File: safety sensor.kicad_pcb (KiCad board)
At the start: 2 copper layers, 99.1 x 45.7 mm, 29 parts, among them IC1 STM8S003F3P6, J1 Conn_01x02, J2 Conn_01x01, J3 Conn_01x01, J4 Conn_01x01, J5 Conn_01x02, J6 Conn_01x01, U1 LD1117V33, U2 VCNL3020-GS08

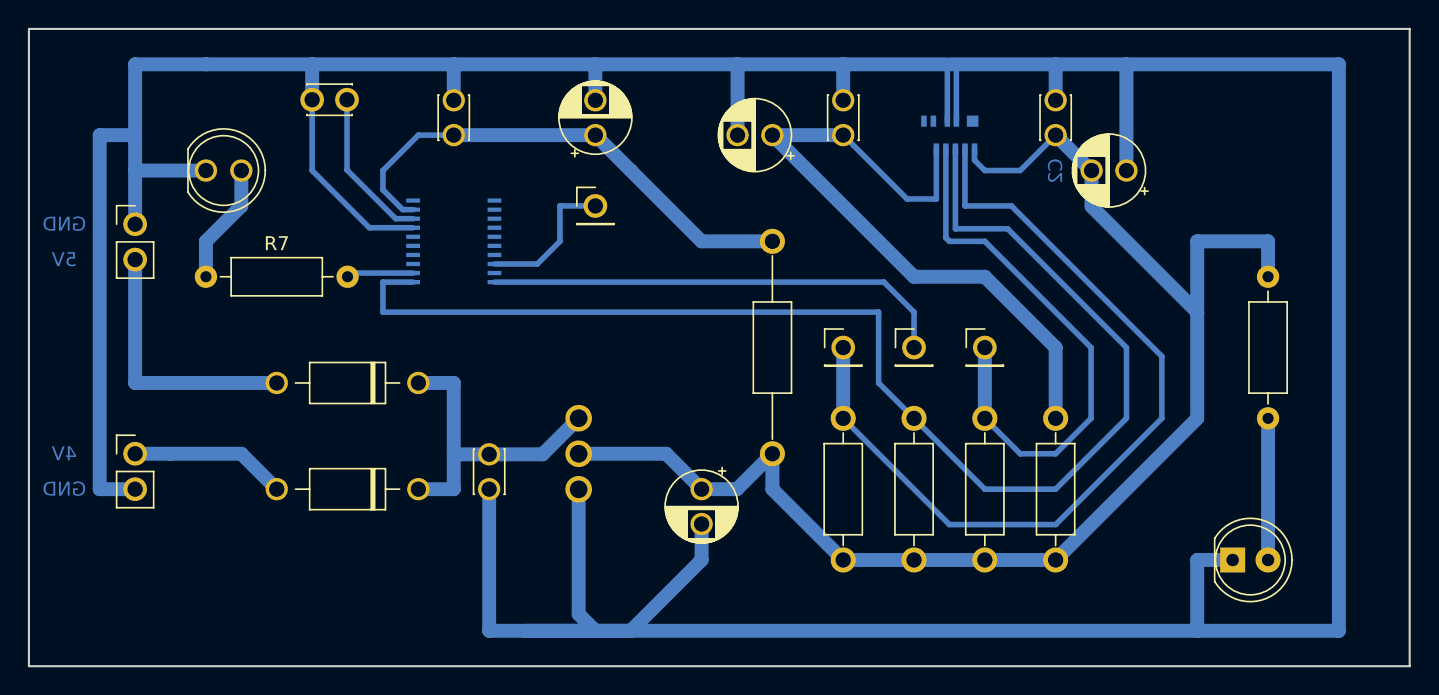
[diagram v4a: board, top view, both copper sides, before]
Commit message: fix c1 polarity, fix the hole sizes
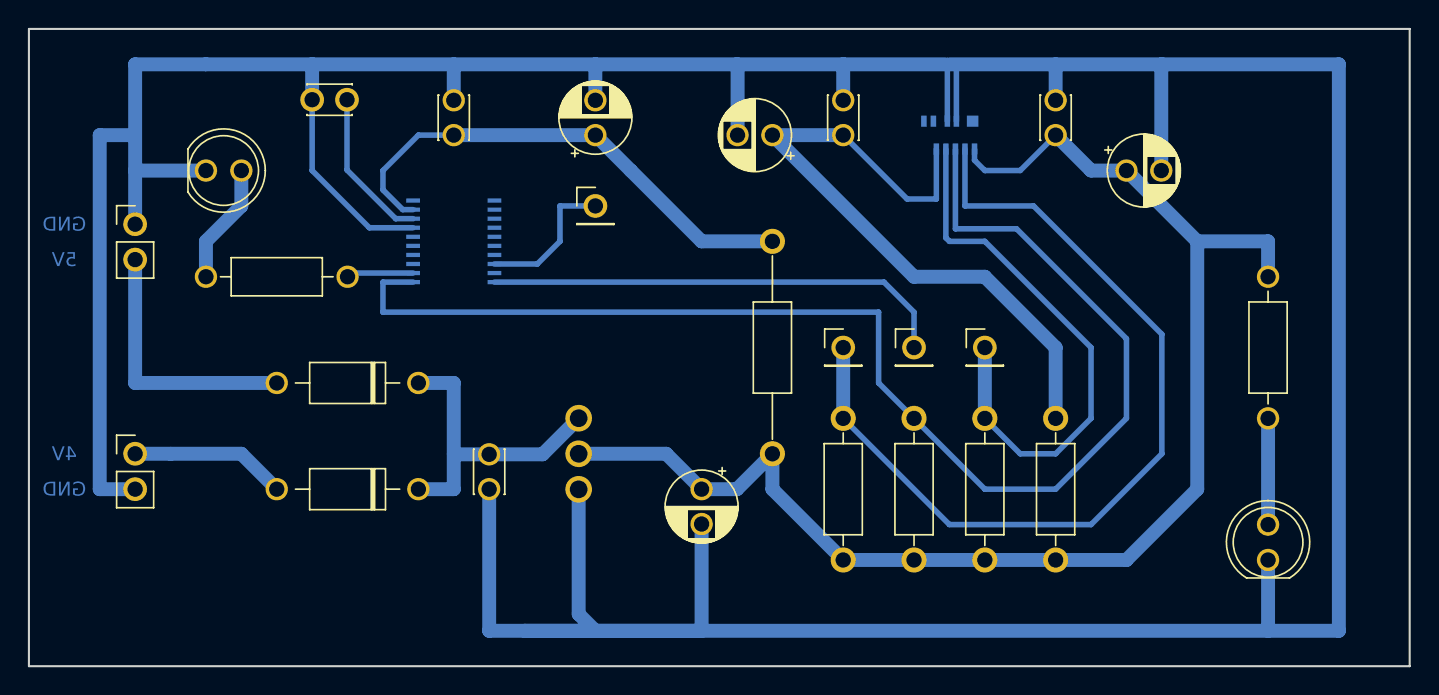
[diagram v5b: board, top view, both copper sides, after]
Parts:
- moved D3 2.54 mm to (106.7, 55.9), turned to 90 degrees
- turned C1 to 0 degrees
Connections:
- C1 pad 1: GND -> +3.3V
- C1 pad 2: +3.3V -> GND
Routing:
- net Net-(D3-Pad2): track 10.2 -> 7.62 mm
- net Net-(J2-Pad1): track 61.4 -> 63.8 mm
- net +3.3V: track 136.9 -> 136.2 mm

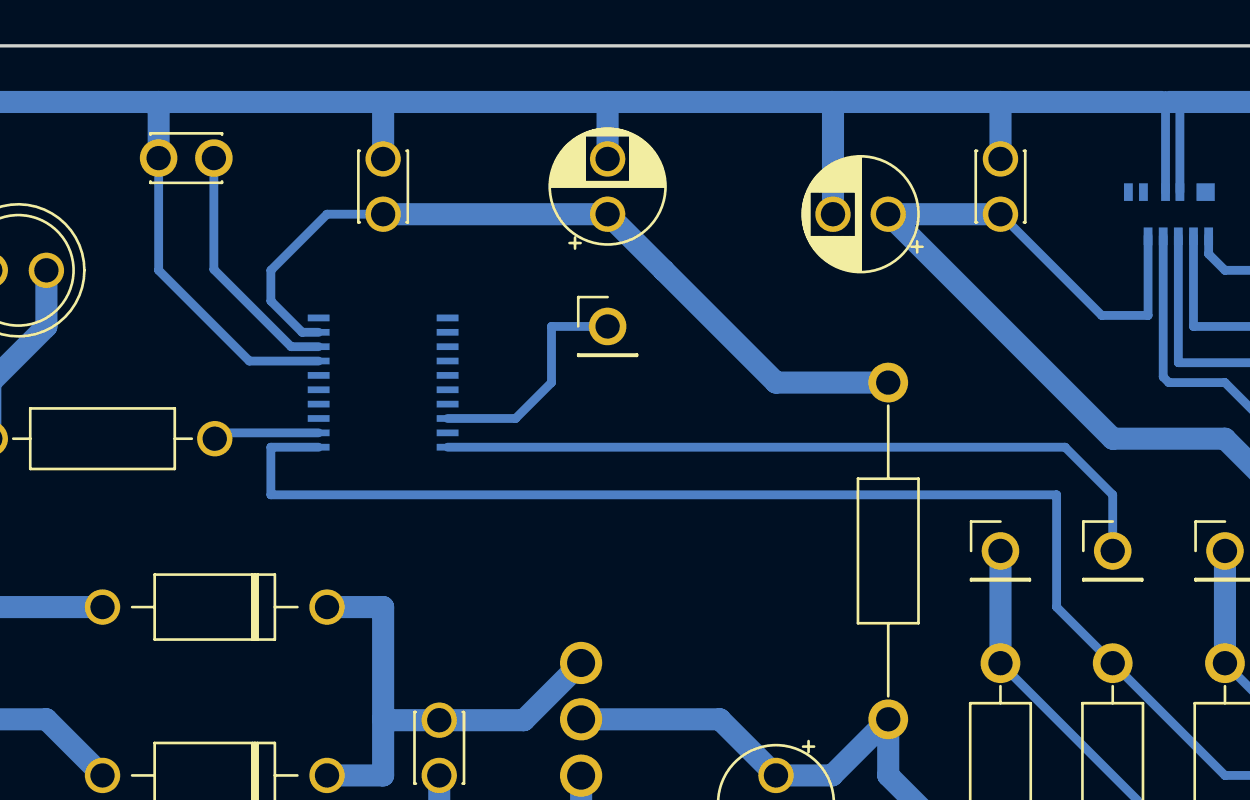
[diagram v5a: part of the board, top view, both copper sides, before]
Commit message: flip stm8 chip, update from updated footrpint and connect it accordingly
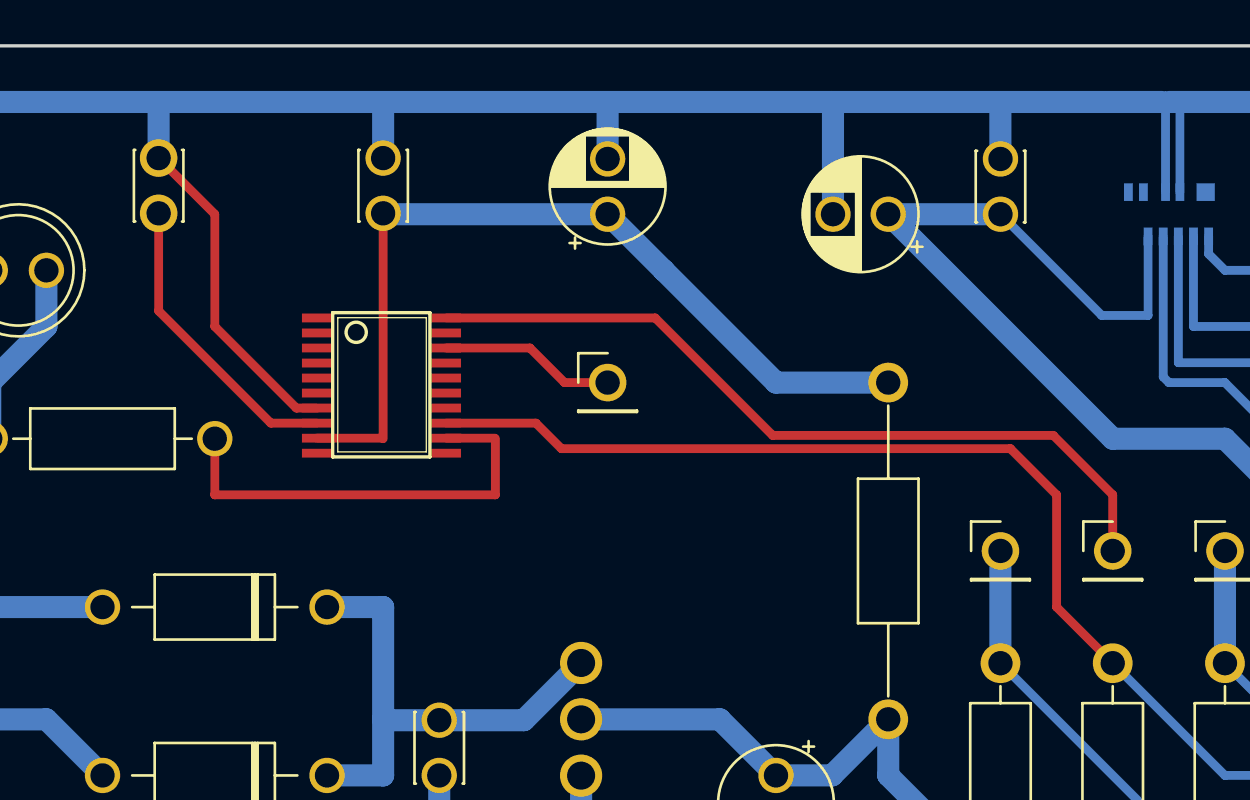
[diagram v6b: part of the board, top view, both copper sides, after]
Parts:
- IC1: moved to F.Cu
- moved J6 2.54 mm to (58.4, 33.0)
- turned C3 to -90 degrees
- turned IC1 to -90 degrees
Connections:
- IC1 pad 1: Net-(IC1-Pad1) -> unconnected-(IC1-Pad1)
- IC1 pad 12: unconnected-(IC1-Pad12) -> Net-(IC1-Pad12)
- IC1 pad 13: unconnected-(IC1-Pad13) -> Net-(R1-Pad1)
- IC1 pad 2: Net-(IC1-Pad2) -> unconnected-(IC1-Pad2)
- R1 pad 1: Net-(IC1-Pad1) -> Net-(R1-Pad1)
- R7 pad 2: Net-(IC1-Pad2) -> Net-(IC1-Pad12)
- U2 pad 3: Net-(IC1-Pad1) -> Net-(R1-Pad1)
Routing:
- net Net-(IC1-Pad1): track 95.0 -> 0.00 mm
- net Net-(R1-Pad1): track 0.00 -> 84.1 mm
- net Net-(IC1-Pad12): track 0.00 -> 20.4 mm
- net Net-(IC1-Pad2): track 4.81 -> 0.00 mm
- net +3.3V: track 136.2 -> 139.2 mm
- net Net-(IC1-Pad18): track 10.5 -> 7.96 mm
- net Net-(IC1-Pad20): track 33.5 -> 36.0 mm
- net Net-(C3-Pad2): track 11.2 -> 13.7 mm
- net GND: track 329.2 -> 330.0 mm

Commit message: fixing track pad connection errors and polishing stm8 tssop20 footprint
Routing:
- net Net-(R7-Pad2): track 20.4 -> 18.5 mm

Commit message: pad name changes in schematic
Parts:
- J2: value Conn_01x01 -> SDA
- J3: value Conn_01x01 -> SCL
- J4: value Conn_01x01 -> INT
- J6: value Conn_01x01 -> SWIM
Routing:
- net Net-(IC1-Pad13): track 84.1 -> 89.5 mm
- net Net-(J3-Pad1): track 39.9 -> 41.4 mm
- net Net-(IC1-Pad12): track 18.5 -> 20.0 mm
- net Net-(C8-Pad1): track 49.0 -> 50.4 mm
- net Net-(J2-Pad1): track 63.8 -> 64.7 mm
